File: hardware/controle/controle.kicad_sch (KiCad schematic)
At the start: 33 parts, among them J3 PWR, J4 DATA, J5 UART7, J6 TWI3, J7 SENS0375, J8 TWI4, J9 LED, U2 MCP7940N-xSN, U4 ULN2003, Y1 32.768Khz

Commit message: Adjust some references and availability
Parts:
- C3: footprint Capacitor_SMD:C_0805_2012Metric_Pad1.18x1.45mm_HandSolder -> Capacitor_SMD:C_0603_1608Metric_Pad1.08x0.95mm_HandSolder; P/N C0805C104K5RACTU -> stock
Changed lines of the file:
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@@
 			)
 		)
-		(property "Footprint" "Capacitor_SMD:C_0805_2012Metric_Pad1.18x1.45mm_HandSolder"
+		(property "Footprint" "Capacitor_SMD:C_0603_1608Metric_Pad1.08x0.95mm_HandSolder"
 			(at 66.04 113.03 0)
 			(effects
@@
 			)
 		)
-		(property "P/N" "C0805C104K5RACTU"
+		(property "P/N" "stock"
 			(at 97.79 63.5 0)
 			(effects

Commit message: hardware/controle: fix sort circuit on RS232 interface
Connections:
- net +3V3: no longer BT1.2 (-), C3.1, C4.2, C5.2, GPIO-2.2, GPIO-2.36, J3.2 (Pin_2), J4.1 (Pin_1), J5.3 (Pin_3), J6.5 (Pin_5), J7.3 (Pin_3), J8.3 (Pin_3), U2.4 (VSS), U4.8 (GND)
- new net GND: BT1.2 (-), C3.1, C4.2, C5.2, GPIO-2.2, J3.2 (Pin_2), J5.3 (Pin_3), J6.5 (Pin_5), J7.3 (Pin_3), J8.3 (Pin_3), U2.4 (VSS), U4.8 (GND)
- new net PI18/UART2_TX: GPIO-2.36, J4.1 (Pin_1)
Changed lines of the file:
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@@
-	)
-	(junction
-		(at 204.47 142.24)
-		(diameter 0)
-		(color 0 0 0 0)
 	)
 	(junction
@@
 	)
 	(junction
-		(at 204.47 139.7)
-		(diameter 0)
-		(color 0 0 0 0)
-	)
-	(junction
 		(at 119.38 55.88)
 		(diameter 0)
@@
 	(wire
 		(pts
-			(xy 144.78 132.08) (xy 190.5 132.08)
+			(xy 144.78 132.08) (xy 187.96 132.08)
 		)
 		(stroke
@@
 	(wire
 		(pts
-			(xy 204.47 149.86) (xy 190.5 149.86)
+			(xy 204.47 149.86) (xy 187.96 149.86)
 		)
 		(stroke
@@
 	(wire
 		(pts
+			(xy 204.47 147.32) (xy 190.5 147.32)
+		)
+		(stroke
+			(width 0)
+			(type default)
+		)
+	)
+	(wire
+		(pts
 			(xy 240.03 38.1) (xy 240.03 53.34)
 		)
@@
 	(wire
 		(pts
+			(xy 190.5 147.32) (xy 190.5 134.62)
+		)
+		(stroke
+			(width 0)
+			(type default)
+		)
+	)
+	(wire
+		(pts
 			(xy 209.55 59.69) (xy 209.55 71.12)
 		)
@@
 	(wire
 		(pts
-			(xy 204.47 134.62) (xy 204.47 139.7)
-		)
-		(stroke
-			(width 0)
-			(type default)
-		)
-	)
-	(wire
-		(pts
 			(xy 219.71 71.12) (xy 220.98 71.12)
 		)
@@
 	(wire
 		(pts
-			(xy 204.47 139.7) (xy 204.47 142.24)
-		)
-		(stroke
-			(width 0)
-			(type default)
-		)
-	)
-	(wire
-		(pts
 			(xy 59.69 102.87) (xy 59.69 115.57)
 		)
@@
 	(wire
 		(pts
-			(xy 144.78 134.62) (xy 204.47 134.62)
+			(xy 144.78 134.62) (xy 190.5 134.62)
 		)
 		(stroke
@@
 	(wire
 		(pts
-			(xy 190.5 149.86) (xy 190.5 132.08)
+			(xy 187.96 149.86) (xy 187.96 132.08)
 		)
 		(stroke
@@
 		)
 		(stroke
-			(width 0)
-			(type default)
-		)
-	)
-	(wire
-		(pts
-			(xy 204.47 142.24) (xy 204.47 147.32)
-		)
-		(stroke

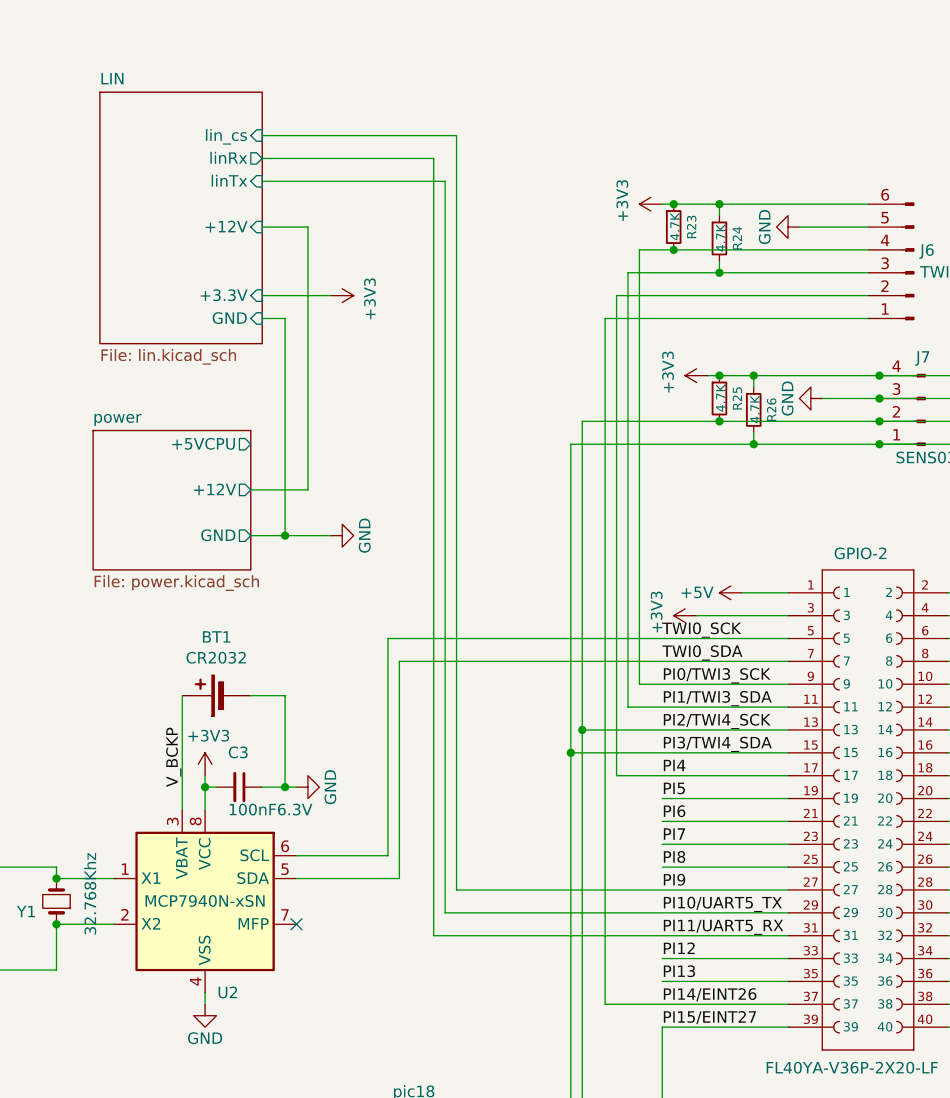
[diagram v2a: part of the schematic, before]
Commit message: controle: add P-MOS transistors to control power to the LIN devices
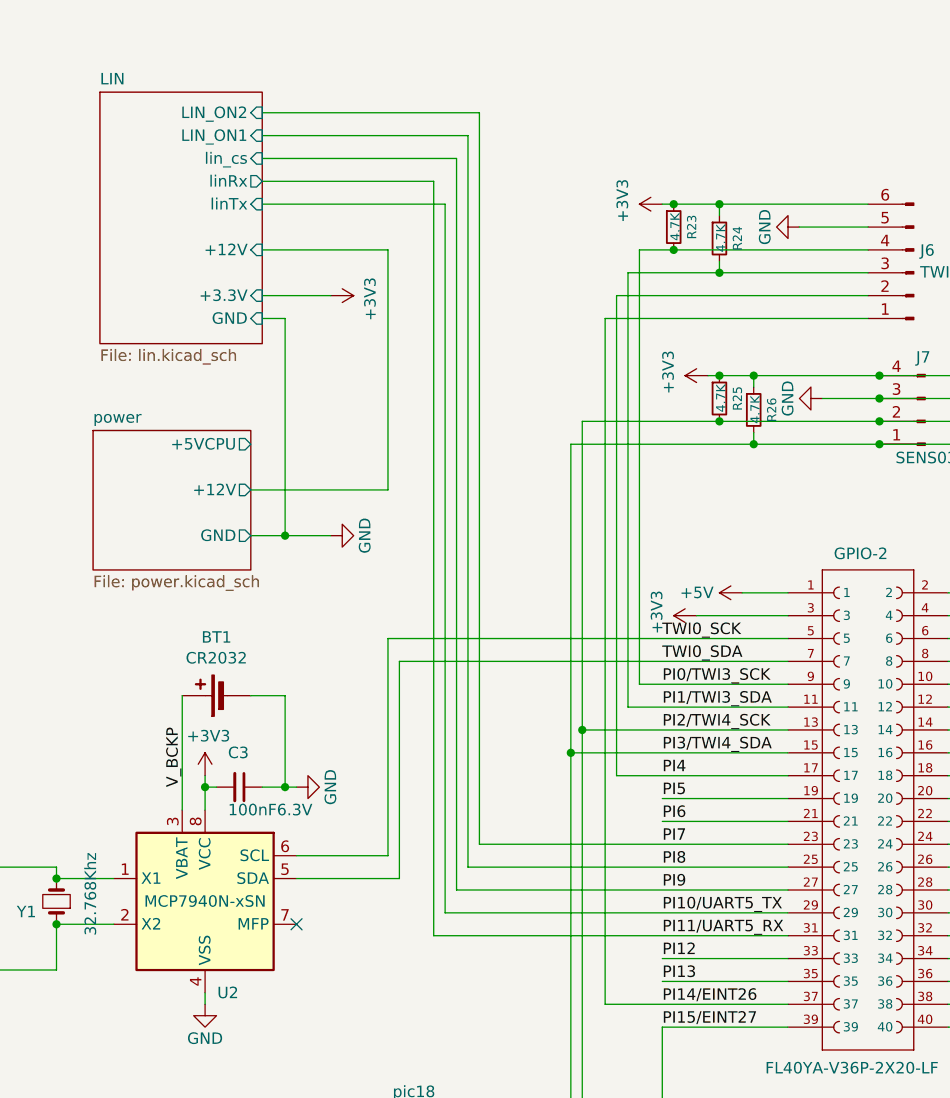
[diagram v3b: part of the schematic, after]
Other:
- sheet LIN ports: added LIN_ON1, LIN_ON2; removed none
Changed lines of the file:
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@@
 	(wire
 		(pts
-			(xy 68.58 45.72) (xy 88.9 45.72)
+			(xy 68.58 48.26) (xy 88.9 48.26)
 		)
 		(stroke
@@
 	(wire
 		(pts
-			(xy 67.31 80.01) (xy 73.66 80.01)
+			(xy 67.31 80.01) (xy 82.55 80.01)
 		)
 		(stroke
@@
 	(wire
 		(pts
-			(xy 68.58 40.64) (xy 90.17 40.64)
+			(xy 68.58 43.18) (xy 90.17 43.18)
 		)
 		(stroke
@@
 	(wire
 		(pts
+			(xy 92.71 119.38) (xy 127 119.38)
+		)
+		(stroke
+			(width 0)
+			(type default)
+		)
+	)
+	(wire
+		(pts
 			(xy 123.19 74.93) (xy 102.87 74.93)
 		)
@@
 	(wire
 		(pts
-			(xy 204.47 149.86) (xy 187.96 149.86)
+			(xy 91.44 121.92) (xy 127 121.92)
 		)
 		(stroke
@@
 	(wire
 		(pts
-			(xy 71.12 60.96) (xy 71.12 85.09)
+			(xy 204.47 149.86) (xy 187.96 149.86)
 		)
 		(stroke
@@
 	(wire
 		(pts
-			(xy 119.38 54.61) (xy 119.38 55.88)
+			(xy 71.12 60.96) (xy 71.12 85.09)
 		)
 		(stroke
@@
 	(wire
 		(pts
-			(xy 123.19 73.66) (xy 123.19 74.93)
+			(xy 119.38 54.61) (xy 119.38 55.88)
 		)
 		(stroke
@@
 	(wire
 		(pts
-			(xy 68.58 43.18) (xy 87.63 43.18)
+			(xy 123.19 73.66) (xy 123.19 74.93)
 		)
 		(stroke
@@
 	(wire
 		(pts
-			(xy 68.58 58.42) (xy 76.2 58.42)
+			(xy 68.58 45.72) (xy 87.63 45.72)
 		)
 		(stroke
@@
 	(wire
 		(pts
-			(xy 113.03 121.92) (xy 127 121.92)
+			(xy 68.58 58.42) (xy 76.2 58.42)
 		)
 		(stroke
@@
 	(wire
 		(pts
+			(xy 68.58 40.64) (xy 91.44 40.64)
+		)
+		(stroke
+			(width 0)
+			(type default)
+		)
+	)
+	(wire
+		(pts
 			(xy 88.9 127) (xy 127 127)
 		)
@@
 	(wire
 		(pts
-			(xy 73.66 50.8) (xy 73.66 80.01)
+			(xy 82.55 53.34) (xy 82.55 80.01)
 		)
 		(stroke
@@
 	(wire
 		(pts
-			(xy 113.03 119.38) (xy 127 119.38)
-		)
-		(stroke
-			(width 0)
-			(type default)
-		)
-	)
-	(wire
-		(pts
 			(xy 220.98 90.17) (xy 219.71 90.17)
 		)
@@
 	(wire
 		(pts
-			(xy 87.63 43.18) (xy 87.63 129.54)
+			(xy 91.44 40.64) (xy 91.44 121.92)
+		)
+		(stroke
+			(width 0)
+			(type default)
+		)
+	)
+	(wire
+		(pts
+			(xy 87.63 45.72) (xy 87.63 129.54)
 		)
 		(stroke
@@
 	(wire
 		(pts
-			(xy 90.17 40.64) (xy 90.17 124.46)
+			(xy 90.17 43.18) (xy 90.17 124.46)
 		)
 		(stroke
@@
 	(wire
 		(pts
+			(xy 68.58 38.1) (xy 92.71 38.1)
+		)
+		(stroke
+			(width 0)
+			(type default)
+		)
+	)
+	(wire
+		(pts
 			(xy 135.89 58.42) (xy 107.95 58.42)
 		)
@@
 	(wire
 		(pts
-			(xy 88.9 45.72) (xy 88.9 127)
+			(xy 88.9 48.26) (xy 88.9 127)
 		)
 		(stroke
@@
 	(wire
 		(pts
-			(xy 68.58 50.8) (xy 73.66 50.8)
+			(xy 68.58 53.34) (xy 82.55 53.34)
 		)
 		(stroke
@@
 	(wire
 		(pts
+			(xy 92.71 38.1) (xy 92.71 119.38)
+		)
+		(stroke
+			(width 0)
+			(type default)
+		)
+	)
+	(wire
+		(pts
 			(xy 175.26 64.77) (xy 175.26 109.22)
 		)
@@
 		)
 		(pin "linRx" output
-			(at 68.58 43.18 0)
+			(at 68.58 45.72 0)
 			(effects
 				(font
@@
 		)
 		(pin "linTx" input
-			(at 68.58 45.72 0)
+			(at 68.58 48.26 0)
 			(effects
 				(font
@@
 		)
 		(pin "+12V" input
-			(at 68.58 50.8 0)
+			(at 68.58 53.34 0)
 			(effects
 				(font
@@
 		)
 		(pin "lin_cs" input
-			(at 68.58 40.64 0)
+			(at 68.58 43.18 0)
 			(effects
 				(font
@@
 			(effects
 				(font
+					(size 1.27 1.27)
+				)
+				(justify right)
+			)
+		)
+		(pin "LIN_ON2" input
+			(at 68.58 38.1 0)
+			(effects
+				(font
+					(size 1.27 1.27)
+				)
+				(justify right)
+			)
+		)
+		(pin "LIN_ON1" input
+			(at 68.58 40.64 0)
+			(effects
+				(font

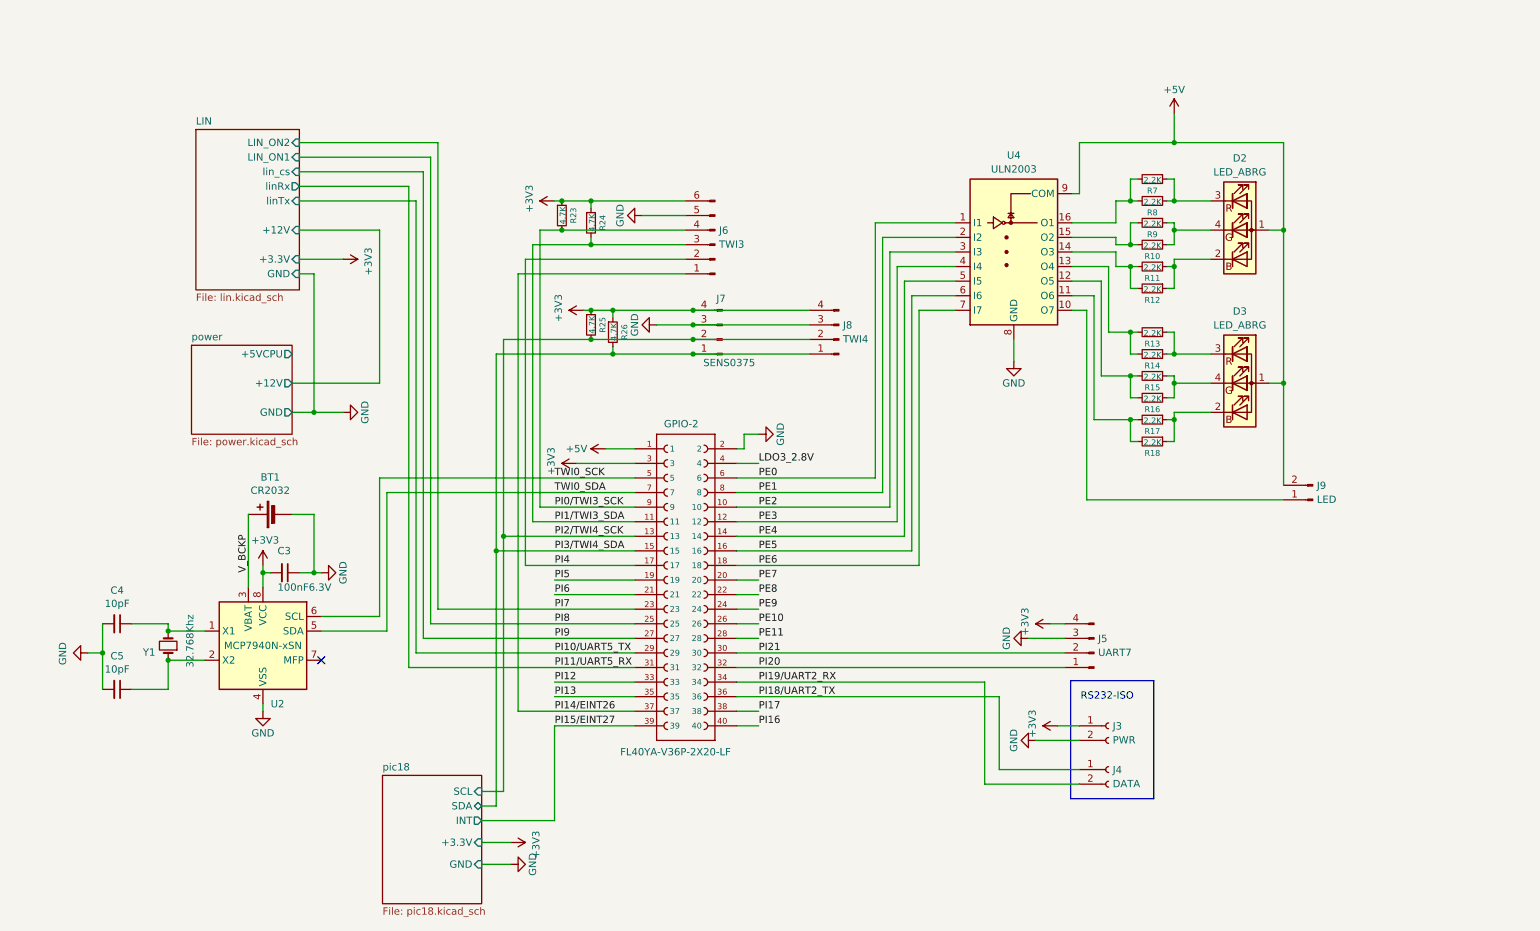
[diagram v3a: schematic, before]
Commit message: controle: - pass ERC - adjust some components and connections - place components on board
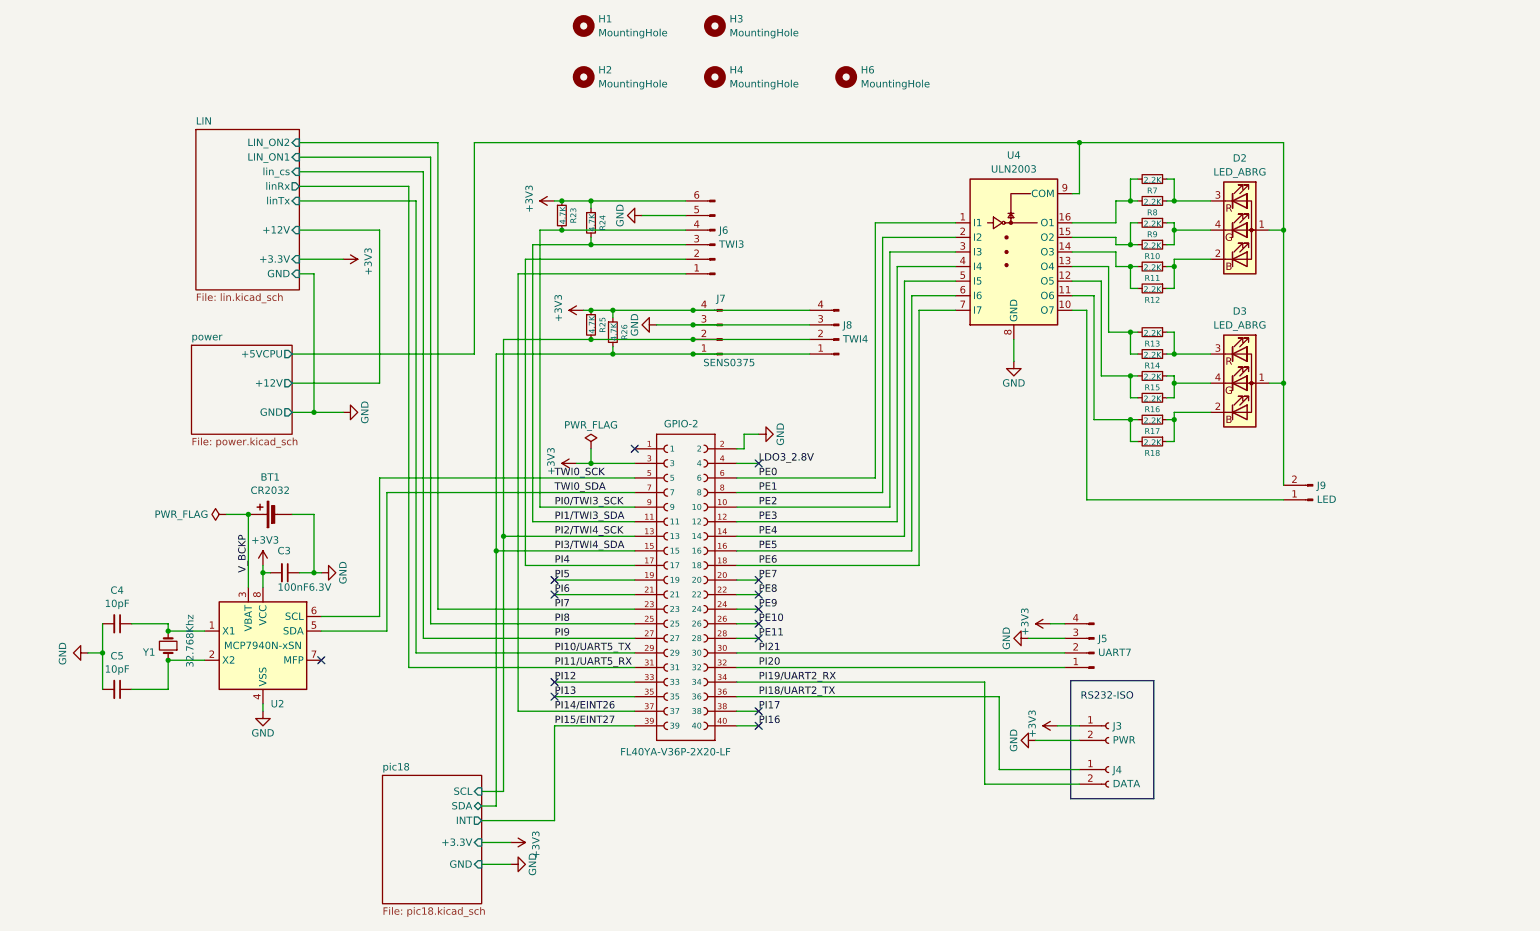
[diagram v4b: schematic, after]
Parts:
- added H1, H2, H3, H4, H6: MountingHole, MountingHole:MountingHole_3.2mm_M3, symbol Mechanical:MountingHole
- GPIO-2: footprint A20_OLIMEXINO_LIME2_SHIELD.mod:A20_OLIMEXINO_LIME2_SHIELD_1-YA-V36P-2X20-LF -> A20_OLIMEXINO_LIME2_SHIELD.mod:A10_OLIMEXINO_LIME_SHIELD_1-YA-V36P-2X20-LF
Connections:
- net power/+5VCPU: now also D2.1 (A), D3.1 (A), J9.2 (Pin_2), U4.9 (COM)
- removed net +5V: D2.1 (A), D3.1 (A), GPIO-2.1, J9.2 (Pin_2), U4.9 (COM)
- no-connect marks 1 -> 14

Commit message: Update LED resistors values. Minor updates to PCB
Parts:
- R10, R12, R14, R16, R18, R8: value 2.2K -> 330
- R11, R13, R15, R17, R7, R9: value 2.2K -> 330; now not fitted
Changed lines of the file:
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@@
 		(in_bom yes)
 		(on_board yes)
-		(dnp no)
+		(dnp yes)
 		(property "Reference" "R11"
 			(at 217.17 61.722 90)
@@
 			)
 		)
-		(property "Value" "2.2K"
+		(property "Value" "330"
 			(at 217.1954 59.8678 90)
 			(effects
@@
 			)
 		)
-		(property "Value" "2.2K"
+		(property "Value" "330"
 			(at 217.1954 75.1078 90)
 			(effects
@@
 		(in_bom yes)
 		(on_board yes)
-		(dnp no)
+		(dnp yes)
 		(property "Reference" "R7"
 			(at 217.17 46.482 90)
@@
 			)
 		)
-		(property "Value" "2.2K"
+		(property "Value" "330"
 			(at 217.1954 44.6278 90)
 			(effects
@@
 			)
 		)
-		(property "Value" "2.2K"
+		(property "Value" "330"
 			(at 217.1954 82.7278 90)
 			(effects
@@
 		(in_bom yes)
 		(on_board yes)
-		(dnp no)
+		(dnp yes)
 		(property "Reference" "R9"
 			(at 217.17 54.102 90)
@@
 			)
 		)
-		(property "Value" "2.2K"
+		(property "Value" "330"
 			(at 217.1954 52.2478 90)
 			(effects
@@
 			)
 		)
-		(property "Value" "2.2K"
+		(property "Value" "330"
 			(at 217.1954 56.0578 90)
 			(effects
@@
 			)
 		)
-		(property "Value" "2.2K"
+		(property "Value" "330"
 			(at 217.1954 90.3478 90)
 			(effects
@@
 		(in_bom yes)
 		(on_board yes)
-		(dnp no)
+		(dnp yes)
 		(property "Reference" "R13"
 			(at 217.17 73.152 90)
@@
 			)
 		)
-		(property "Value" "2.2K"
+		(property "Value" "330"
 			(at 217.1954 71.2978 90)
 			(effects
@@
 		(in_bom yes)
 		(on_board yes)
-		(dnp no)
+		(dnp yes)
 		(property "Reference" "R15"
 			(at 217.17 80.772 90)
@@
 			)
 		)
-		(property "Value" "2.2K"
+		(property "Value" "330"
 			(at 217.1954 78.9178 90)
 			(effects
@@
 			)
 		)
-		(property "Value" "2.2K"
+		(property "Value" "330"
 			(at 217.1954 63.6778 90)
 			(effects
@@
 			)
 		)
-		(property "Value" "2.2K"
+		(property "Value" "330"
 			(at 217.1954 48.4378 90)
 			(effects
@@
 		(in_bom yes)
 		(on_board yes)
-		(dnp no)
+		(dnp yes)
 		(property "Reference" "R17"
 			(at 217.17 88.392 90)
@@
 			)
 		)
-		(property "Value" "2.2K"
+		(property "Value" "330"
 			(at 217.1954 86.5378 90)
 			(effects

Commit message: hardware/controle: adjust RGB leds resistors
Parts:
- R10, R16: value 330 -> 1k
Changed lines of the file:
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@@
 			)
 		)
-		(property "Value" "330"
+		(property "Value" "1k"
 			(at 217.1954 82.7278 90)
 			(effects
@@
 			)
 		)
-		(property "Value" "330"
+		(property "Value" "1k"
 			(at 217.1954 56.0578 90)
 			(effects

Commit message: hardware/controle: add fiducials (for OpenPnP)
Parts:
- added FID1, FID2, FID3, FID4, FID5, FID6: Fiducial, Fiducial:Fiducial_1mm_Mask2mm, symbol Mechanical:Fiducial
